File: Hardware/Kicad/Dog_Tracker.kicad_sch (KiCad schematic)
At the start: 20 parts, among them IC1 M4 Feather, U1 ADP160AUJZ-1.8-R7, U2 SX1280IMLTRT, U3 Origin_GPS1510, U4 NFA18SL407V1A45L, U5 SN74AUP1T97, U6 LSM6DSO32

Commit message: 'wire i2c'
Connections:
- net I2C_SCL: no longer IC1.27 (SCL)
- net I2C_SDA: no longer IC1.28 (SDA)
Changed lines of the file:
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@@
+    (stroke (width 0) (type default) (color 0 0 0 0))
+  )
+  (wire (pts (xy 171.45 60.325) (xy 192.405 60.325))
     (stroke (width 0) (type default) (color 0 0 0 0))
   )
@@
     (stroke (width 0) (type default) (color 0 0 0 0))
   )
+  (wire (pts (xy 276.86 73.025) (xy 276.86 149.225))
+    (stroke (width 0) (type default) (color 0 0 0 0))
+  )
   (wire (pts (xy 121.285 47.625) (xy 121.285 75.565))
     (stroke (width 0) (type default) (color 0 0 0 0))
@@
     (stroke (width 0) (type default) (color 0 0 0 0))
   )
+  (wire (pts (xy 195.58 57.785) (xy 195.58 70.485))
+    (stroke (width 0) (type default) (color 0 0 0 0))
+  )
   (wire (pts (xy 184.785 123.19) (xy 184.785 109.855))
     (stroke (width 0) (type default) (color 0 0 0 0))
@@
     (stroke (width 0) (type default) (color 0 0 0 0))
   )
+  (wire (pts (xy 272.415 70.485) (xy 272.415 145.415))
+    (stroke (width 0) (type default) (color 0 0 0 0))
+  )
   (wire (pts (xy 259.715 137.795) (xy 253.365 137.795))
     (stroke (width 0) (type default) (color 0 0 0 0))
@@
     (stroke (width 0) (type default) (color 0 0 0 0))
   )
+  (wire (pts (xy 192.405 60.325) (xy 192.405 73.025))
+    (stroke (width 0) (type default) (color 0 0 0 0))
+  )
   (wire (pts (xy 95.25 80.645) (xy 118.11 80.645))
     (stroke (width 0) (type default) (color 0 0 0 0))
@@
     (stroke (width 0) (type default) (color 0 0 0 0))
   )
+  (wire (pts (xy 171.45 57.785) (xy 195.58 57.785))
+    (stroke (width 0) (type default) (color 0 0 0 0))
+  )
   (wire (pts (xy 130.175 87.63) (xy 163.83 87.63))
     (stroke (width 0) (type default) (color 0 0 0 0))
@@
     (stroke (width 0) (type default) (color 0 0 0 0))
   )
+  (wire (pts (xy 195.58 70.485) (xy 272.415 70.485))
+    (stroke (width 0) (type default) (color 0 0 0 0))
+  )
+  (wire (pts (xy 276.86 149.225) (xy 216.535 149.225))
+    (stroke (width 0) (type default) (color 0 0 0 0))
+  )
   (wire (pts (xy 128.905 34.925) (xy 128.905 47.625))
     (stroke (width 0) (type default) (color 0 0 0 0))
@@
     (stroke (width 0) (type default) (color 0 0 0 0))
   )
+  (wire (pts (xy 192.405 73.025) (xy 276.86 73.025))
+    (stroke (width 0) (type default) (color 0 0 0 0))
+  )
   (wire (pts (xy 81.915 40.005) (xy 114.935 40.005))
     (stroke (width 0) (type default) (color 0 0 0 0))
@@
   )
   (wire (pts (xy 102.235 63.5) (xy 102.235 70.485))
+    (stroke (width 0) (type default) (color 0 0 0 0))
+  )
+  (wire (pts (xy 272.415 145.415) (xy 253.365 145.415))
     (stroke (width 0) (type default) (color 0 0 0 0))
   )
@@
     (effects (font (size 1.27 1.27)) (justify left bottom))
   )
-  (text "VTL: Convert from 1.8V to 3.3V" (at 230.505 151.765 0)
+  (text "VTL: Convert from 1.8V to 3.3V" (at 231.14 155.575 0)
     (effects (font (size 1.27 1.27) (thickness 0.254) bold) (justify left bottom))
   )
@@
     (effects (font (size 1.27 1.27)) (justify left bottom))
   )
-  (global_label "I2C_SDA" (shape input) (at 216.535 149.225 0) (fields_autoplaced)
-    (effects (font (size 1.27 1.27)) (justify left))
-    (property "Intersheet References" "${INTERSHEET_REFS}" (id 0) (at 226.5681 149.1456 0)
-      (effects (font (size 1.27 1.27)) (justify left) hide)
-    )
+  (label "I2C_SCL" (at 187.325 57.785 0)
+    (effects (font (size 1.27 1.27)) (justify left bottom))
+  )
+  (label "I2C_SDA" (at 229.87 73.025 0)
+    (effects (font (size 1.27 1.27)) (justify left bottom))
   )
   (global_label "WAKEUP_GPS" (shape input) (at 140.335 52.705 180) (fields_autoplaced)
@@
     )
   )
-  (global_label "I2C_SCL" (shape input) (at 253.365 145.415 0) (fields_autoplaced)
-    (effects (font (size 1.27 1.27)) (justify left))
-    (property "Intersheet References" "${INTERSHEET_REFS}" (id 0) (at 263.3376 145.3356 0)
-      (effects (font (size 1.27 1.27)) (justify left) hide)
-    )
-  )
   (global_label "PED_CS" (shape input) (at 170.815 45.085 0) (fields_autoplaced)
     (effects (font (size 1 1)) (justify left))
@@
     )
   )
-  (global_label "I2C_SCL" (shape input) (at 170.815 57.785 0) (fields_autoplaced)
-    (effects (font (size 1.27 1.27)) (justify left))
-    (property "Intersheet References" "${INTERSHEET_REFS}" (id 0) (at 180.7876 57.7056 0)
-      (effects (font (size 1.27 1.27)) (justify left) hide)
-    )
-  )
   (global_label "~{RESET}" (shape output) (at 170.815 40.005 0) (fields_autoplaced)
     (effects (font (size 1.27 1.27)) (justify left))
@@
     )
   )
-  (global_label "I2C_SDA" (shape input) (at 170.815 60.325 0) (fields_autoplaced)
-    (effects (font (size 1.27 1.27)) (justify left))
-    (property "Intersheet References" "${INTERSHEET_REFS}" (id 0) (at 180.8481 60.2456 0)
-      (effects (font (size 1.27 1.27)) (justify left) hide)
-    )
-  )

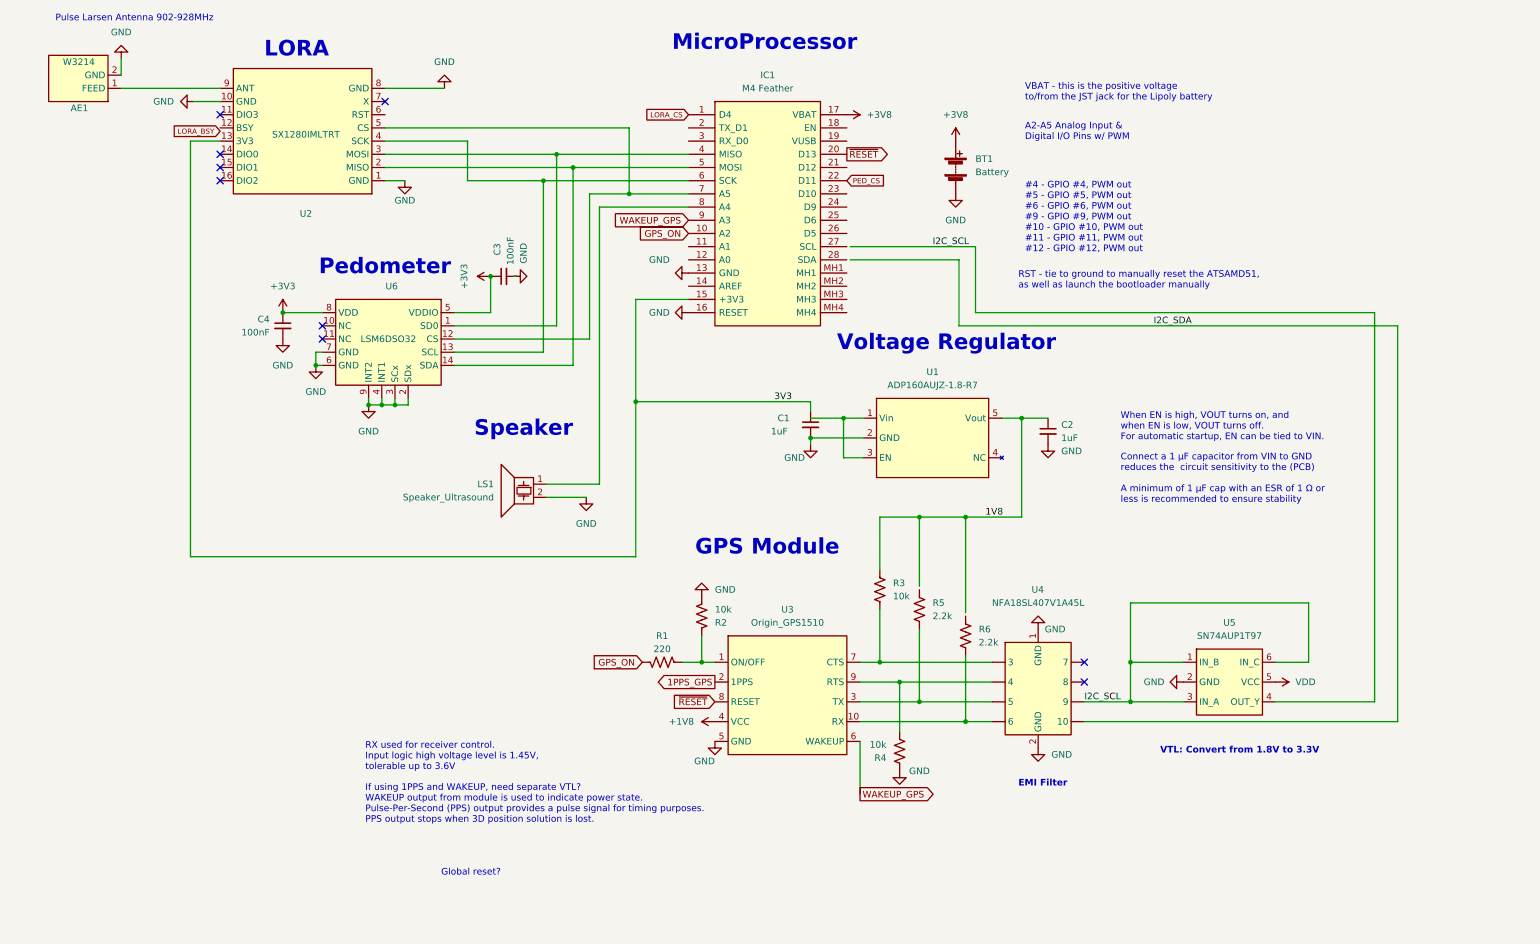
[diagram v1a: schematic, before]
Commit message: schematic fixed
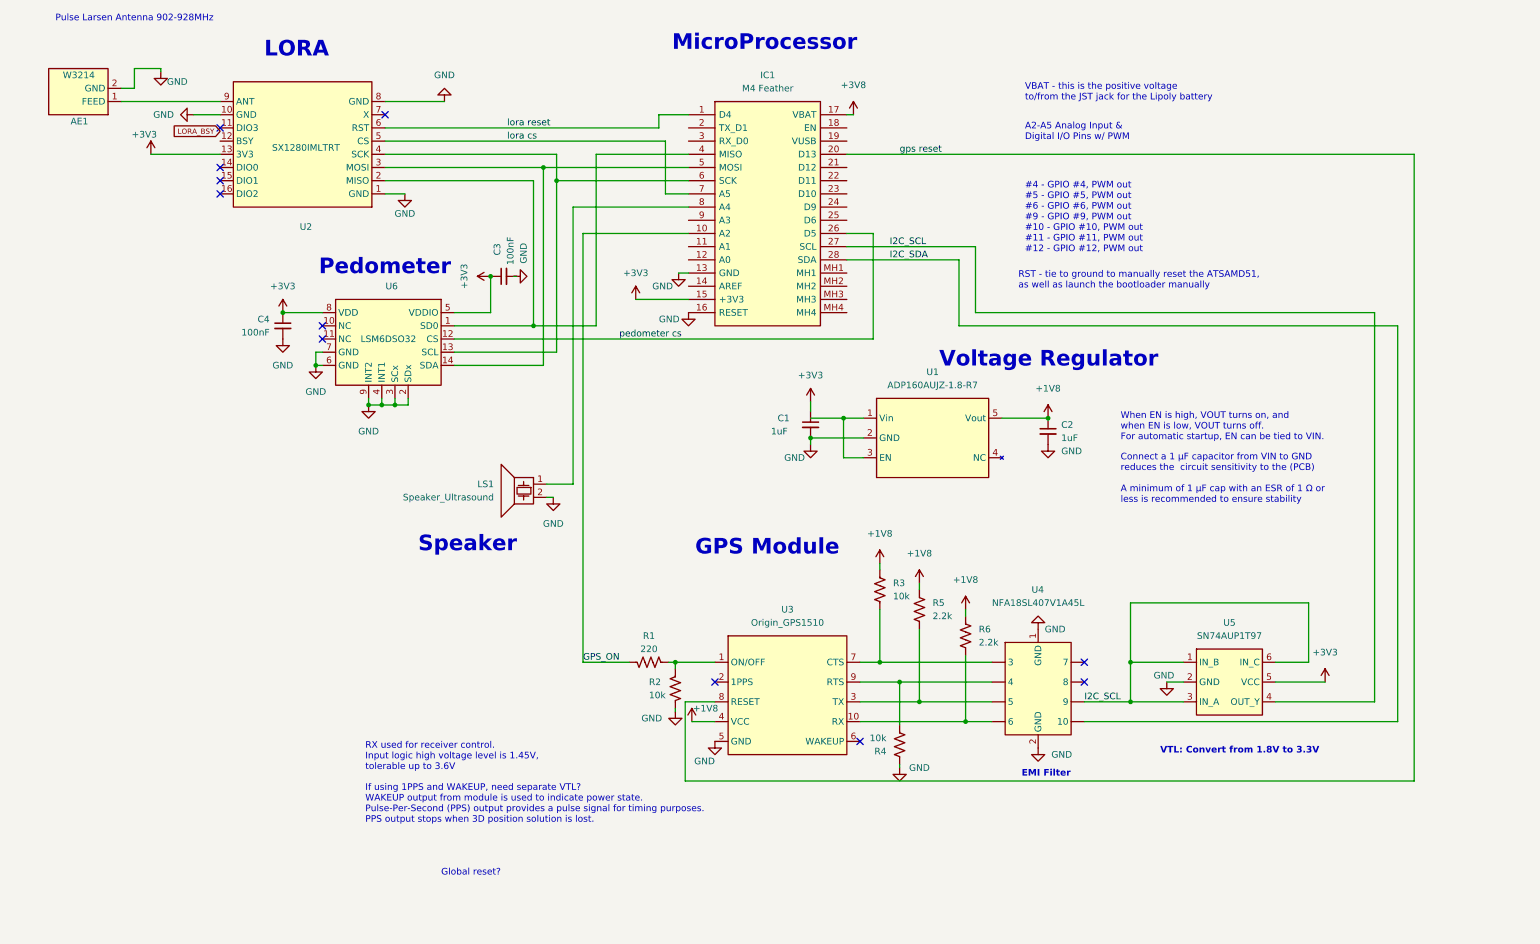
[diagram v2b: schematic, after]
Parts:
- removed BT1: Battery, symbol Device:Battery
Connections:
- net 1V8 is gone; now on net +1V8: C2.1, R3.2, U1.5 (Vout)
- net 3V3 is gone; now on net +3V3: C1.1, IC1.15 (+3V3), U2.13 (3V3)
- net LORA_CS is gone; now on net lora reset: IC1.1 (D4)
- net VDD is gone; now on net +3V3: U5.5 (VCC)
- net +1V8: now also R5.2, R6.2
- net I2C_SCL: now also IC1.27 (SCL)
- net I2C_SDA: now also IC1.28 (SDA)
- net at IC1.5 (MOSI), U6.14 (SDA): now also U2.3 (MOSI); no longer U2.2 (MISO)
- net at IC1.4 (MISO), U6.1 (SD0): now also U2.2 (MISO); no longer U2.3 (MOSI)
- net lora cs: now reaches IC1.7 (A5), U2.5 (CS)
- net lora cs: no longer U6.12 (CS)
- net lora reset: now reaches U2.6 (RST)
- net pedometer cs: now reaches IC1.26 (D5)
- net pedometer cs: now also U6.12 (CS)
- net 1PPS_GPS: no longer names the net of U3.2 (1PPS)
- net PED_CS: no longer names the net of IC1.22 (D11)
- net WAKEUP_GPS: no longer names the net of U3.6 (WAKEUP)
- net WAKEUP_GPS: no longer IC1.9 (A3)
- net ~{RESET} renamed gps reset
- no-connect marks 9 -> 11
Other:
- moved on the sheet: AE1, R1, R2, R4, U2

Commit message: 'fixed erc, need to fix warnings'
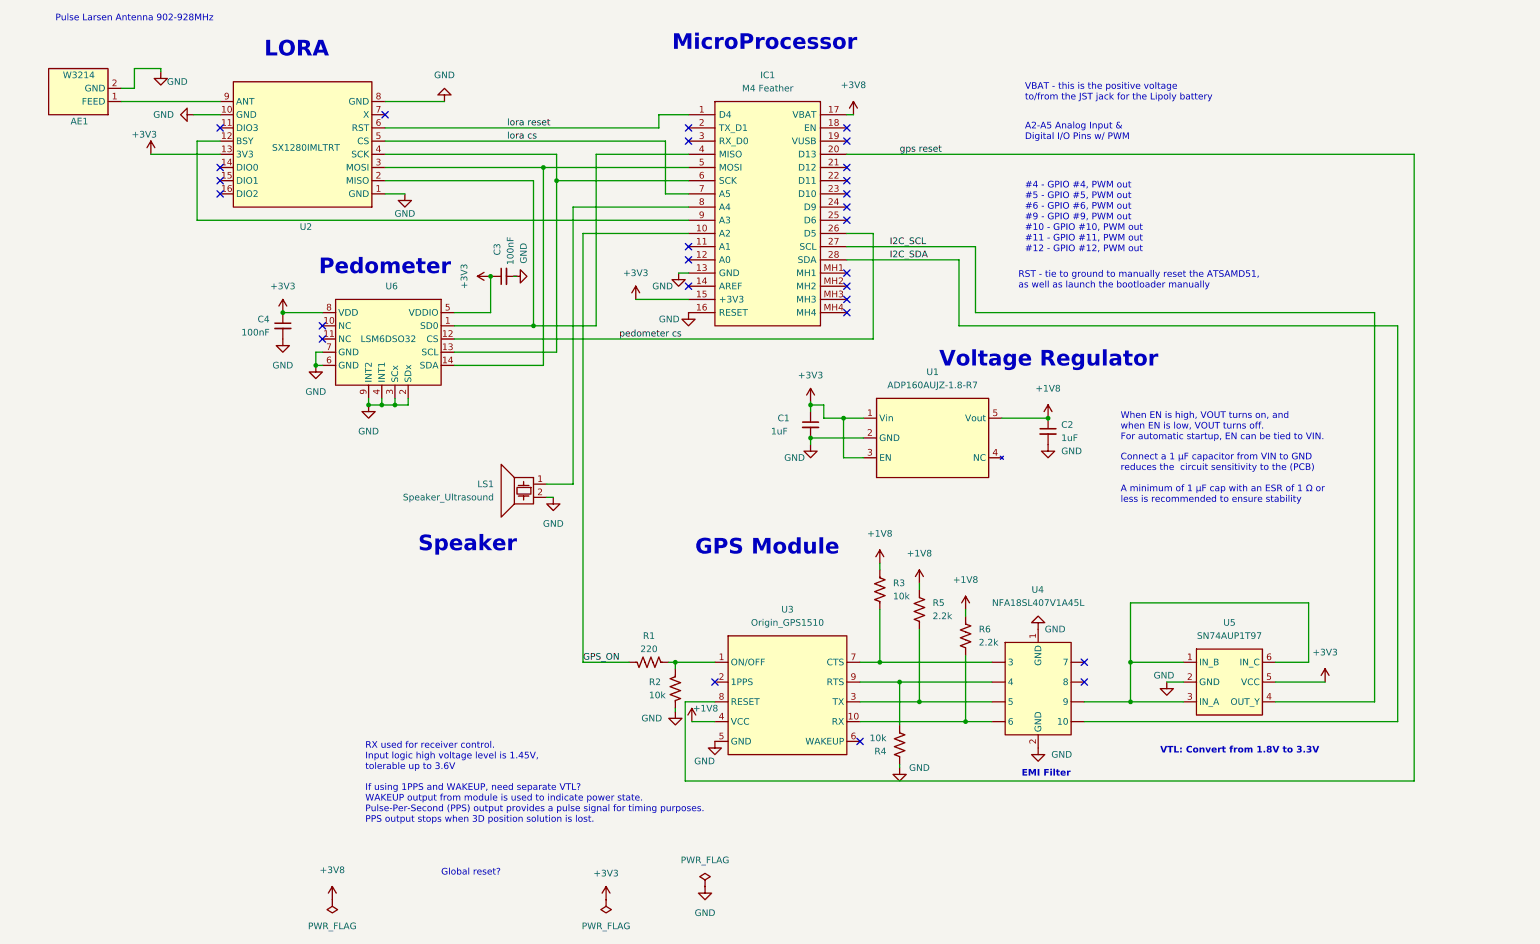
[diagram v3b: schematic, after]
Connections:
- net +3V3: now also U1.1 (Vin), U1.3 (EN)
- net I2C_SCL: no longer U4. (9), U5.1 (IN_B), U5.3 (IN_A), U5.6 (IN_C)
- net at U2.12 (BSY): now also IC1.9 (A3)
- new net: U4. (9), U5.1 (IN_B), U5.3 (IN_A), U5.6 (IN_C)
- no-connect marks 11 -> 27

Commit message: no errors, no warnings
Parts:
- AE1: symbol DogTracker:W3214 -> Dog_Tracker:W3214
- IC1: footprint Dog_Tracker:M4Feather -> 3857; symbol DogTracker:M4 Feather -> Dog_Tracker:M4 Feather
- U1: symbol DogTracker:ADP160AUJZ-2.8-R7 -> Dog_Tracker:ADP160AUJZ-1.8-R7
- U2: symbol DogTracker:SX1280IMLTRT_Radio -> Dog_Tracker:SX1280IMLTRT_Radio
- U3: symbol DogTracker:Origin_GPS1510 -> Dog_Tracker:Origin_GPS1510
- U4: symbol DogTracker:NFA18SL407V1A45L -> Dog_Tracker:NFA18SL407V1A45L
- U5: symbol DogTracker:SN74AUP1T97 -> Dog_Tracker:SN74AUP1T97
- U6: symbol DogTracker:LSM6DSO32 -> Dog_Tracker:LSM6DSRTR
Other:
- moved on the sheet: U1, U4

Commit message: footprint speaker
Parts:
- LS1: footprint (none) -> Dog_Tracker:W-03A
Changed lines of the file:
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@@
       (effects (font (size 1.27 1.27)) (justify left))
     )
-    (property "Footprint" "" (id 2) (at 108.839 104.775 0)
+    (property "Footprint" "Dog_Tracker:W-03A" (id 2) (at 108.839 104.775 0)
       (effects (font (size 1.27 1.27)) hide)
     )
@@
     )
     (path "/42b2a1f3-180d-403b-b90d-f6dcca840918"
-      (reference "LS1") (unit 1) (value "Speaker_Ultrasound") (footprint "")
+      (reference "LS1") (unit 1) (value "Speaker_Ultrasound") (footprint "Dog_Tracker:W-03A")
     )
     (path "/2d6a4f0e-aa68-4d44-9390-8ea258fa2bc4"
